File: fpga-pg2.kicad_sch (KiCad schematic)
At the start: 1 part, among them U6 XC7A15T-CSG325

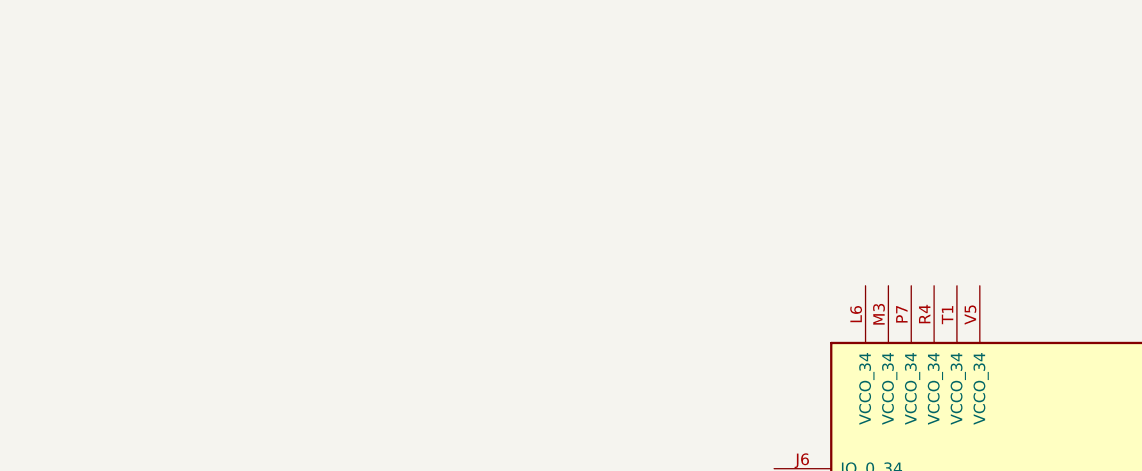
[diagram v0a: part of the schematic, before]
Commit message: placed decoupling caps for fpga
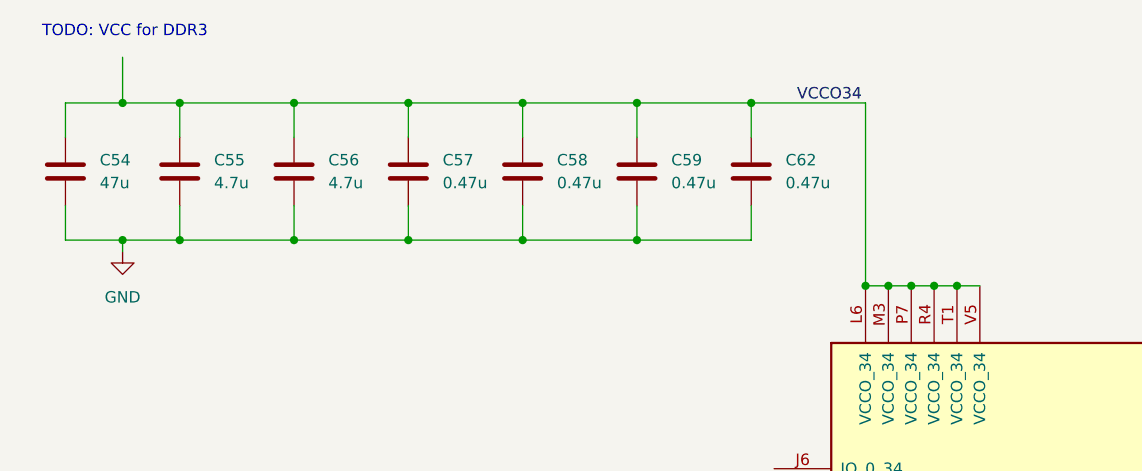
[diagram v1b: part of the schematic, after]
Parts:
- added C54: 47u, Capacitor_SMD:C_1210_3225Metric, symbol Device:C
- added C55, C56: 4.7u, Capacitor_SMD:C_0402_1005Metric, symbol Device:C
- added C57, C58, C59, C62: 0.47u, Capacitor_SMD:C_0402_1005Metric, symbol Device:C
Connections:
- net VCCO34: now reaches U6.L6 (VCCO_34)
- net VCCO34: now also U6.M3 (VCCO_34), U6.P7 (VCCO_34), U6.R4 (VCCO_34), U6.T1 (VCCO_34), U6.V5 (VCCO_34), C54.1, C55.1, C56.1, C57.1, C58.1, C59.1, C62.1
- new net GND: C54.2, C55.2, C56.2, C57.2, C58.2, C59.2, C62.2
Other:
- note added: "TODO: VCC for DDR3"

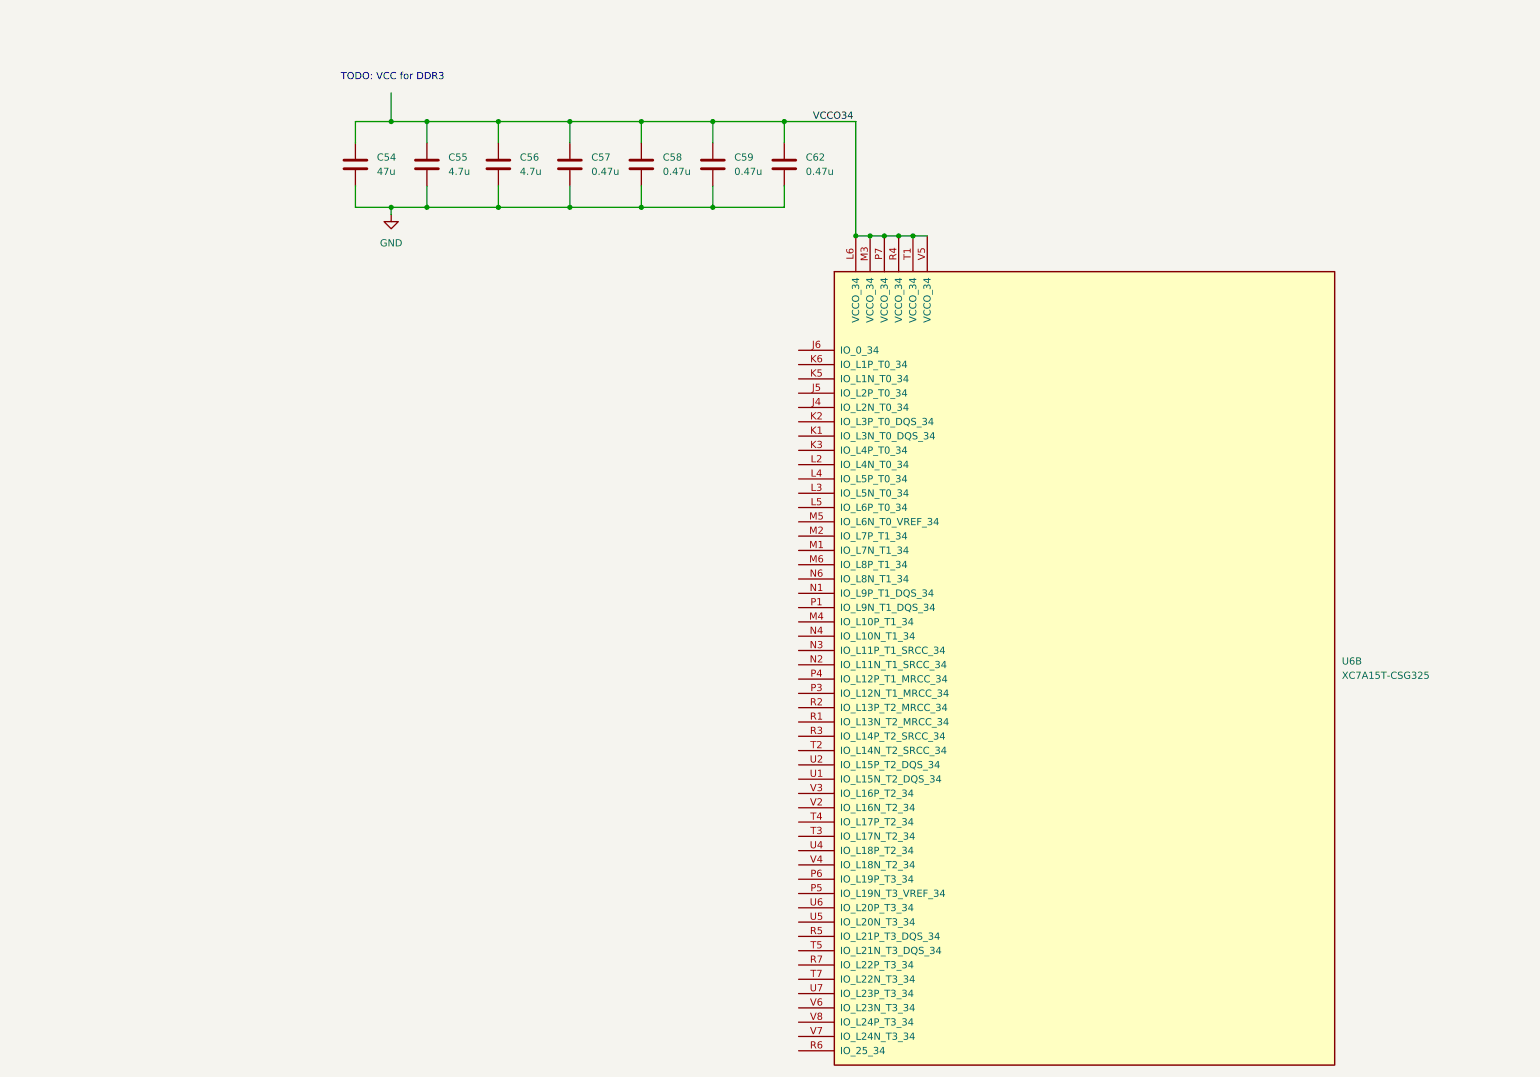
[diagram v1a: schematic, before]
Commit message: started changing package, added correct decoupling
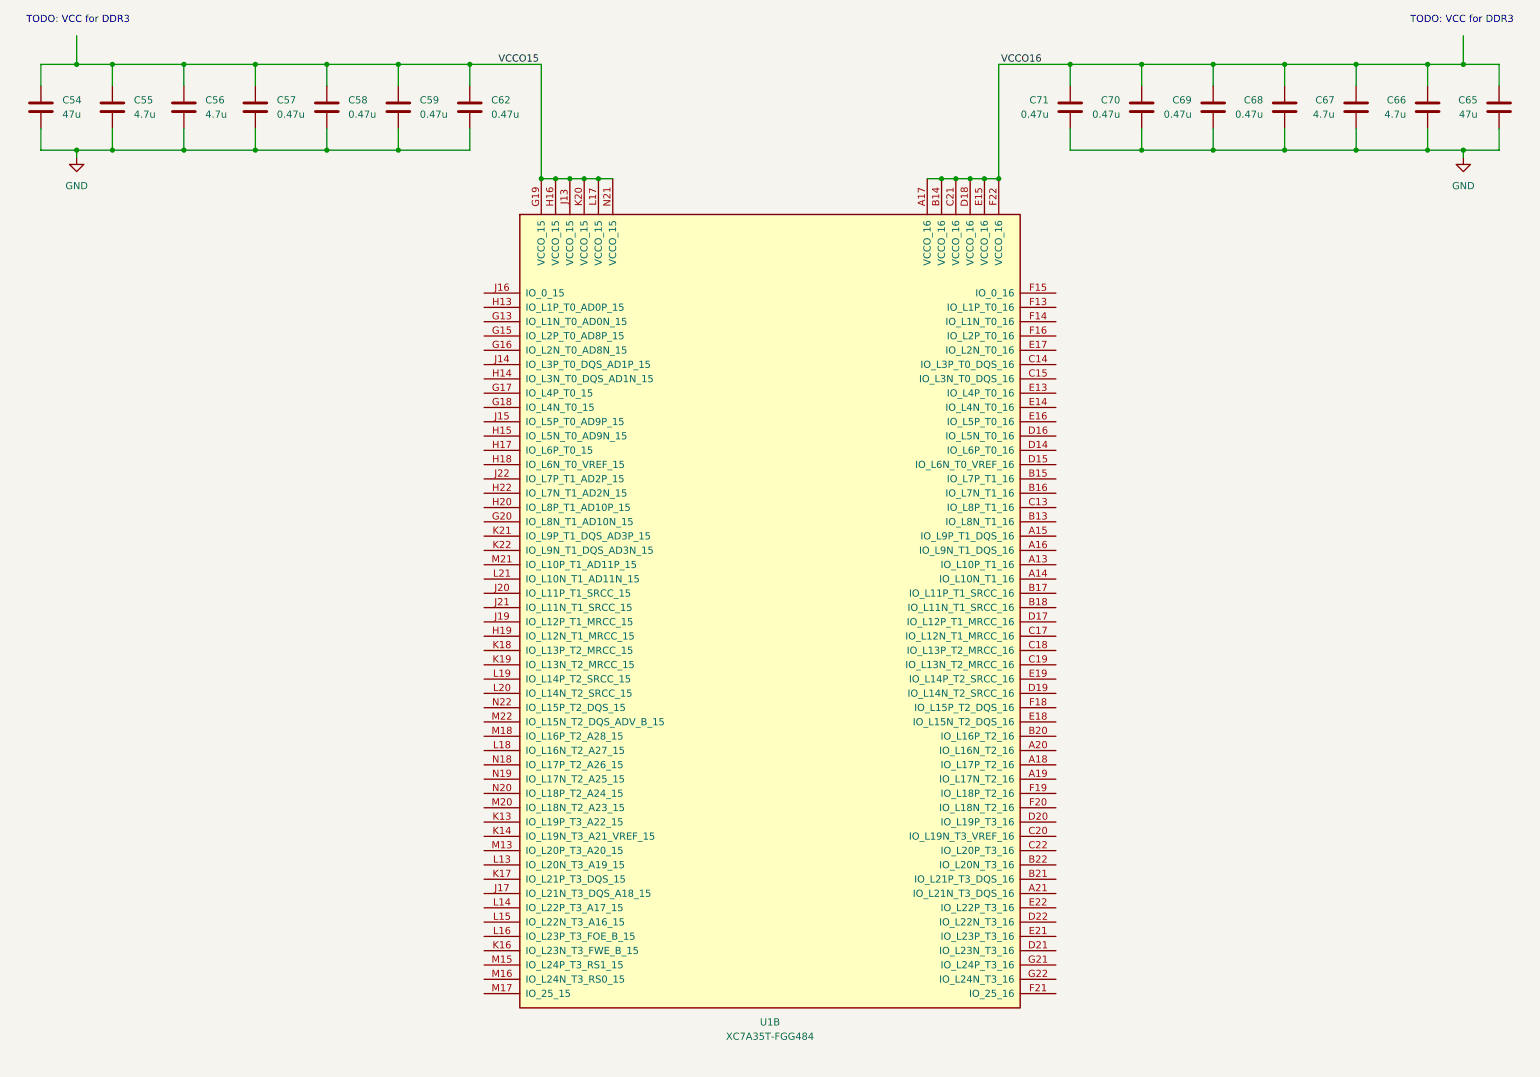
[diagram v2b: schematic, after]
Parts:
- removed U6: XC7A15T-CSG325, Package_BGA:Xilinx_CSG325, symbol FPGA_Xilinx_Artix7:XC7A15T-CSG325
- added C65: 47u, Capacitor_SMD:C_1210_3225Metric, symbol Device:C
- added C66, C67: 4.7u, Capacitor_SMD:C_0402_1005Metric, symbol Device:C
- added C68, C69, C70, C71: 0.47u, Capacitor_SMD:C_0402_1005Metric, symbol Device:C
- added U1: XC7A35T-FGG484, Package_BGA:Xilinx_FGG484, symbol FPGA_Xilinx_Artix7:XC7A35T-FGG484
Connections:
- net GND: now also C65.2, C66.2, C67.2, C68.2, C69.2, C70.2, C71.2
- net VCCO34 renamed VCCO15
- net VCCO15: now also U1.G19 (VCCO_15), U1.H16 (VCCO_15), U1.J13 (VCCO_15), U1.K20 (VCCO_15), U1.L17 (VCCO_15), U1.N21 (VCCO_15)
- new net VCCO16: C65.1, C66.1, C67.1, C68.1, C69.1, C70.1, C71.1, U1.A17 (VCCO_16), U1.B14 (VCCO_16), U1.C21 (VCCO_16), U1.D18 (VCCO_16), U1.E15 (VCCO_16), U1.F22 (VCCO_16)
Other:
- moved on the sheet: C54, C55, C56, C57, C58, C59, C62

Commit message: filled out back connector, finished ddr pinning according to vivado
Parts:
- added TP17, TP18, TP19, TP20, TP21, TP22, TP23, TP24, TP25, TP26, TP27, TP28, TP29, TP30, TP31, TP32, TP49, TP50, TP51, TP52, TP53, TP54, TP55, TP56, TP57, TP58, TP59, TP60, TP61, TP62, TP63, TP64, TP65, TP66, TP67, TP68, TP69, TP70, TP71, TP72, TP73, TP74, TP75, TP76, TP77, TP78, TP79, TP80: TestPoint_Small, symbol Connector:TestPoint_Small
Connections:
- net DI.DI10+: now reaches U1.A13 (IO_L10P_T1_16)
- net DI.DI10+: now also TP67.1
- net DI.DI10-: now reaches U1.A14 (IO_L10N_T1_16)
- net DI.DI10-: now also TP68.1
- net DI.DI9+: now reaches U1.A15 (IO_L9P_T1_DQS_16)
- net DI.DI9+: now also TP65.1
- net DI.DI9-: now reaches U1.A16 (IO_L9N_T1_DQS_16)
- net DI.DI9-: now also TP66.1
- net DO.DO1+: now reaches U1.A18 (IO_L17P_T2_16)
- net DO.DO1+: now also TP17.1
- net DO.DO1-: now reaches U1.A19 (IO_L17N_T2_16)
- net DO.DO1-: now also TP18.1
- net DI.DI16-: now reaches U1.A20 (IO_L16N_T2_16)
- net DI.DI16-: now also TP80.1
- net DO.DO5-: now reaches U1.A21 (IO_L21N_T3_DQS_16)
- net DO.DO5-: now also TP26.1
- net DI.DI8-: now reaches U1.B13 (IO_L8N_T1_16)
- net DI.DI8-: now also TP64.1
- net DI.DI7+: now reaches U1.B15 (IO_L7P_T1_16)
- net DI.DI7+: now also TP61.1
- net DI.DI7-: now reaches U1.B16 (IO_L7N_T1_16)
- net DI.DI7-: now also TP62.1
- net DI.DI11+: now reaches U1.B17 (IO_L11P_T1_SRCC_16)
- net DI.DI11+: now also TP69.1
- net DI.DI11-: now reaches U1.B18 (IO_L11N_T1_SRCC_16)
- net DI.DI11-: now also TP70.1
- net DI.DI16+: now reaches U1.B20 (IO_L16P_T2_16)
- net DI.DI16+: now also TP79.1
- net DO.DO5+: now reaches U1.B21 (IO_L21P_T3_DQS_16)
- net DO.DO5+: now also TP25.1
- net DO.DO4-: now reaches U1.B22 (IO_L20N_T3_16)
- net DO.DO4-: now also TP24.1
- net DI.DI8+: now reaches U1.C13 (IO_L8P_T1_16)
- net DI.DI8+: now also TP63.1
- net DI.DI3+: now reaches U1.C14 (IO_L3P_T0_DQS_16)
- net DI.DI3+: now also TP53.1
- net DI.DI3-: now reaches U1.C15 (IO_L3N_T0_DQS_16)
- net DI.DI3-: now also TP54.1
- net DI.DI12-: now reaches U1.C17 (IO_L12N_T1_MRCC_16)
- net DI.DI12-: now also TP72.1
- net DI.DI13+: now reaches U1.C18 (IO_L13P_T2_MRCC_16)
- net DI.DI13+: now also TP73.1
- net DI.DI13-: now reaches U1.C19 (IO_L13N_T2_MRCC_16)
- net DI.DI13-: now also TP74.1
- net DO.DO3-: now reaches U1.C20 (IO_L19N_T3_VREF_16)
- net DO.DO3-: now also TP22.1
- net DO.DO4+: now reaches U1.C22 (IO_L20P_T3_16)
- net DO.DO4+: now also TP23.1
- net DI.DI6+: now reaches U1.D14 (IO_L6P_T0_16)
- net DI.DI6+: now also TP59.1
- net DI.DI6-: now reaches U1.D15 (IO_L6N_T0_VREF_16)
- net DI.DI6-: now also TP60.1
- net DI.DI5-: now reaches U1.D16 (IO_L5N_T0_16)
- net DI.DI5-: now also TP58.1
- net DI.DI12+: now reaches U1.D17 (IO_L12P_T1_MRCC_16)
- net DI.DI12+: now also TP71.1
- net DI.DI14-: now reaches U1.D19 (IO_L14N_T2_SRCC_16)
- net DI.DI14-: now also TP76.1
- net DO.DO3+: now reaches U1.D20 (IO_L19P_T3_16)
- net DO.DO3+: now also TP21.1
- net DO.DO7-: now reaches U1.D21 (IO_L23N_T3_16)
- net DO.DO7-: now also TP30.1
- net DO.DO6-: now reaches U1.D22 (IO_L22N_T3_16)
- net DO.DO6-: now also TP28.1
- net DI.DI4+: now reaches U1.E13 (IO_L4P_T0_16)
- net DI.DI4+: now also TP55.1
- net DI.DI4-: now reaches U1.E14 (IO_L4N_T0_16)
- net DI.DI4-: now also TP56.1
- net DI.DI5+: now reaches U1.E16 (IO_L5P_T0_16)
- net DI.DI5+: now also TP57.1
- net DI.DI2-: now reaches U1.E17 (IO_L2N_T0_16)
- net DI.DI2-: now also TP52.1
- net DI.DI15-: now reaches U1.E18 (IO_L15N_T2_DQS_16)
- net DI.DI15-: now also TP78.1
- net DI.DI14+: now reaches U1.E19 (IO_L14P_T2_SRCC_16)
- net DI.DI14+: now also TP75.1
- net DO.DO7+: now reaches U1.E21 (IO_L23P_T3_16)
- net DO.DO7+: now also TP29.1
- net DO.DO6+: now reaches U1.E22 (IO_L22P_T3_16)
- net DO.DO6+: now also TP27.1
- net DI.DI1+: now reaches U1.F13 (IO_L1P_T0_16)
- net DI.DI1+: now also TP49.1
- net DI.DI1-: now reaches U1.F14 (IO_L1N_T0_16)
- net DI.DI1-: now also TP50.1
- net DI.DI2+: now reaches U1.F16 (IO_L2P_T0_16)
- net DI.DI2+: now also TP51.1
- net DI.DI15+: now reaches U1.F18 (IO_L15P_T2_DQS_16)
- net DI.DI15+: now also TP77.1
- net DO.DO2+: now reaches U1.F19 (IO_L18P_T2_16)
- net DO.DO2+: now also TP19.1
- net DO.DO2-: now reaches U1.F20 (IO_L18N_T2_16)
- net DO.DO2-: now also TP20.1
- net DO.DO8+: now reaches U1.G21 (IO_L24P_T3_16)
- net DO.DO8+: now also TP31.1
- net DO.DO8-: now reaches U1.G22 (IO_L24N_T3_16)
- net DO.DO8-: now also TP32.1
- net DDR3_REFCLK: now reaches U1.L19 (IO_L14P_T2_SRCC_15)

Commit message: added a lot of stuff
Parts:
- renumbered C54 to C15, C55 to C16, C56 to C17, C57 to C18, C58 to C19, C59 to C20, C62 to C21, C71 to C22, C70 to C23, C69 to C24, C68 to C25, C67 to C26, C66 to C27, C65 to C28, TP49 to TP1, TP58 to TP10, TP59 to TP11, TP60 to TP12, TP61 to TP13, TP62 to TP14, TP63 to TP15, TP64 to TP16, TP65 to TP17, TP66 to TP18, TP67 to TP19, TP50 to TP2, TP68 to TP20, TP69 to TP21, TP70 to TP22, TP71 to TP23, TP72 to TP24, TP73 to TP25, TP74 to TP26, TP75 to TP27, TP76 to TP28, TP77 to TP29, TP51 to TP3, TP78 to TP30, TP79 to TP31, TP80 to TP32, TP17 to TP33, TP18 to TP34, TP19 to TP35, TP20 to TP36, TP21 to TP37, TP22 to TP38, TP23 to TP39, TP52 to TP4, TP24 to TP40, TP25 to TP41, TP26 to TP42, TP27 to TP43, TP28 to TP44, TP29 to TP45, TP30 to TP46, TP31 to TP47, TP32 to TP48, TP53 to TP5, TP54 to TP6, TP55 to TP7, TP56 to TP8, TP57 to TP9

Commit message: did alot of stuff
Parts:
- C15, C28: footprint Capacitor_SMD:C_1210_3225Metric -> Capacitor_SMD:C_1206_3216Metric; LCSC (none) -> C96123
- C16, C17, C26, C27: LCSC (none) -> C23733
- C18, C19, C20, C21, C22, C23, C24, C25: LCSC (none) -> C47339
- TP1, TP10, TP11, TP12, TP13, TP14, TP15, TP16, TP17, TP18, TP19, TP2, TP20, TP21, TP22, TP23, TP24, TP25, TP26, TP27, TP28, TP29, TP3, TP30, TP31, TP32, TP33, TP34, TP35, TP36, TP37, TP38, TP39, TP4, TP40, TP41, TP42, TP43, TP44, TP45, TP46, TP47, TP48, TP5, TP6, TP7, TP8, TP9: now not fitted
- U1: LCSC (none) -> C1521727
